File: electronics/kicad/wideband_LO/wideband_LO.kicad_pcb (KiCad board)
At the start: 2 copper layers, 27 parts, among them U1 BFP620

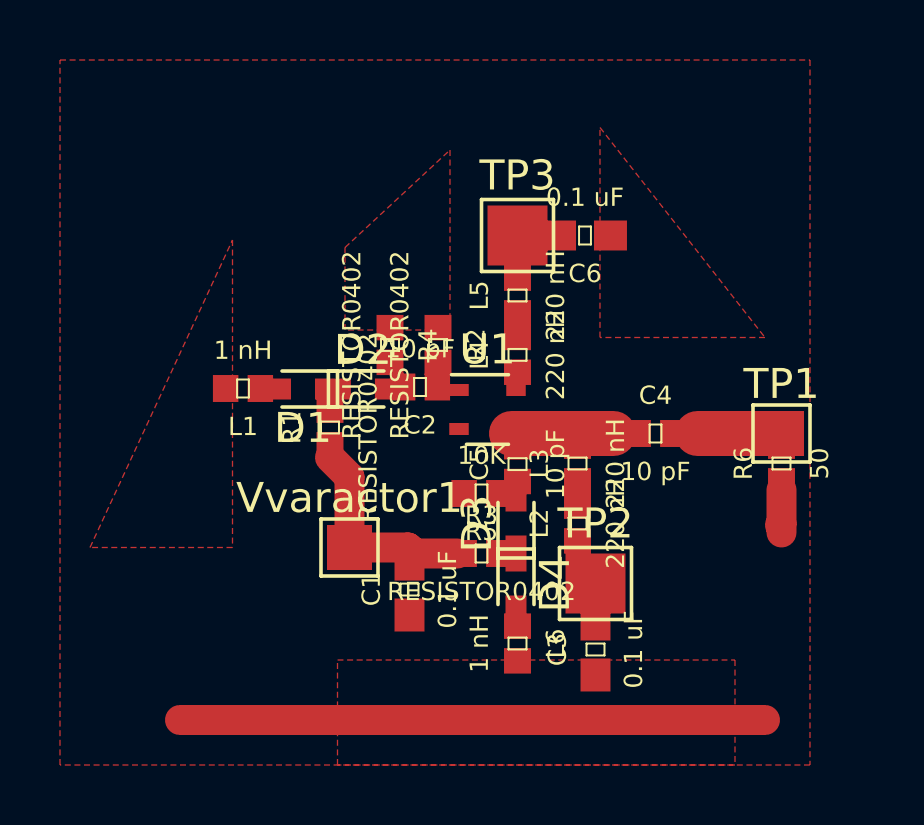
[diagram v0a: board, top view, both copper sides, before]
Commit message: Removed a few otherwise ignored parameters from the diode model
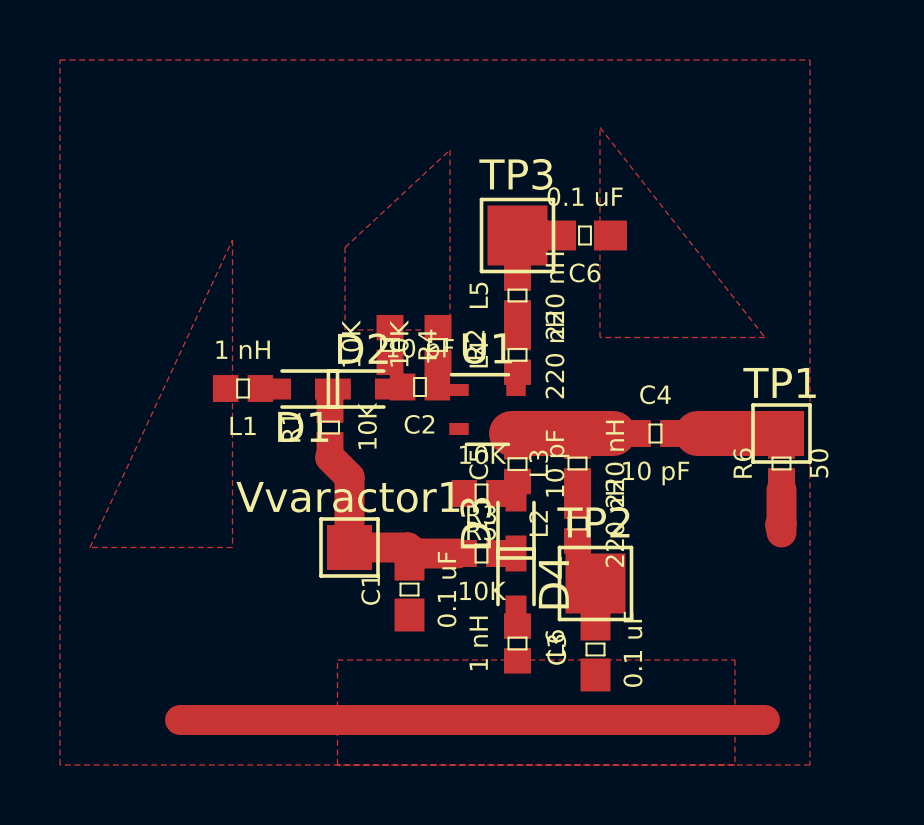
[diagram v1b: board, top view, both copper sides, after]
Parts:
- R1, R2, R3, R4: value RESISTOR0402 -> 10K
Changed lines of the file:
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@@
       (effects (font (size 0.6096 0.6096) (thickness 0.127)))
     )
-    (fp_text value RESISTOR0402 (at 0 1.27 90) (layer F.SilkS)
+    (fp_text value 10K (at 0 1.27 90) (layer F.SilkS)
       (effects (font (size 0.6096 0.6096) (thickness 0.127)))
     )
@@
       (effects (font (size 0.6096 0.6096) (thickness 0.127)))
     )
-    (fp_text value RESISTOR0402 (at 0 1.27) (layer F.SilkS)
+    (fp_text value 10K (at 0 1.27) (layer F.SilkS)
       (effects (font (size 0.6096 0.6096) (thickness 0.127)))
     )
@@
       (effects (font (size 0.6096 0.6096) (thickness 0.127)))
     )
-    (fp_text value RESISTOR0402 (at 0 1.27 90) (layer F.SilkS)
+    (fp_text value 10K (at 0 1.27 90) (layer F.SilkS)
       (effects (font (size 0.6096 0.6096) (thickness 0.127)))
     )
@@
       (effects (font (size 0.6096 0.6096) (thickness 0.127)))
     )
-    (fp_text value RESISTOR0402 (at 0 1.27 90) (layer F.SilkS)
+    (fp_text value 10K (at 0 1.27 90) (layer F.SilkS)
       (effects (font (size 0.6096 0.6096) (thickness 0.127)))
     )

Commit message: Sources still shorting
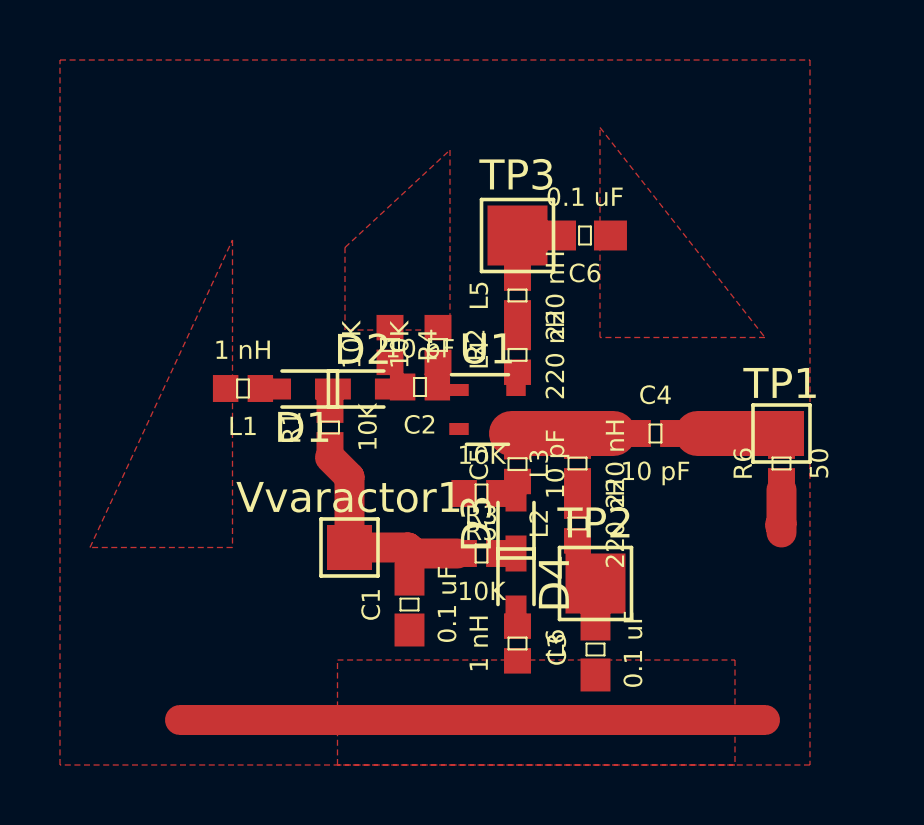
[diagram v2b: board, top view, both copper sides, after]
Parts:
- TP1: value Vemitter -> Voutput
- Vvaractor1: value Vvaractor -> (none)
- moved C1 0.50 mm to (95.4, 103.9)
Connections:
- net Net-(C3-Pad2) renamed nsource
- net Net-(C4-Pad2) renamed noutput
- net Net-(C6-Pad2) renamed nemitter
- net Vvaractor renamed nvaractor

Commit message: Sim runs: ports not rotated.
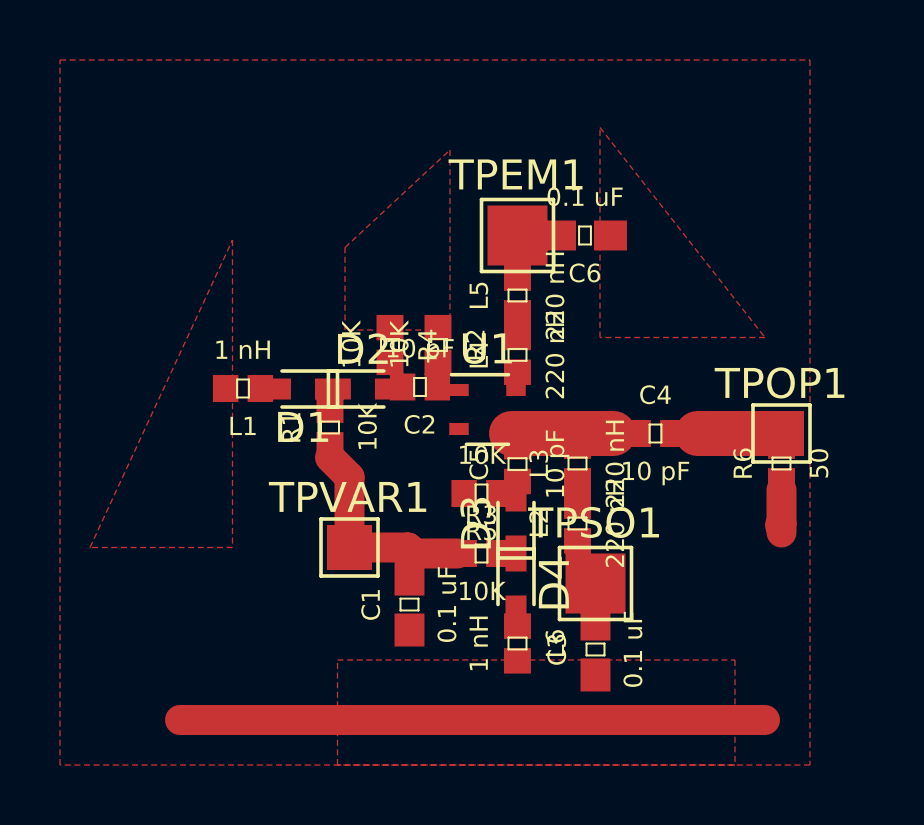
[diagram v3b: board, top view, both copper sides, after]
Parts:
- renumbered TP3 to TPEM1, TP1 to TPOP1, TP2 to TPSO1, Vvaractor1 to TPVAR1
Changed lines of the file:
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@@
     (tags "test point SMD pad rectangle square")
     (attr virtual)
-    (fp_text reference Vvaractor1 (at 0 -1.648) (layer F.SilkS)
+    (fp_text reference TPVAR1 (at 0 -1.648) (layer F.SilkS)
       (effects (font (size 1 1) (thickness 0.15)))
     )
@@
     (tags "test point SMD pad rectangle square")
     (attr virtual)
-    (fp_text reference TP3 (at 0 -1.998) (layer F.SilkS)
+    (fp_text reference TPEM1 (at 0 -1.998) (layer F.SilkS)
       (effects (font (size 1 1) (thickness 0.15)))
     )
@@
     (tags "test point SMD pad rectangle square")
     (attr virtual)
-    (fp_text reference TP2 (at 0 -1.998) (layer F.SilkS)
+    (fp_text reference TPSO1 (at 0 -1.998) (layer F.SilkS)
       (effects (font (size 1 1) (thickness 0.15)))
     )
@@
     (tags "test point SMD pad rectangle square")
     (attr virtual)
-    (fp_text reference TP1 (at 0 -1.648) (layer F.SilkS)
-      (effects (font (size 1 1) (thickness 0.15)))
-    )
+    (fp_text reference TPOP1 (at 0 -1.648) (layer F.SilkS)
+      (effects (font (size 1 1) (thickness 0.15)))
+    )
